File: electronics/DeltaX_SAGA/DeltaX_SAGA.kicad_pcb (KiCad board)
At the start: 4 copper layers, 50 x 50 mm, 76 parts, among them J1 USB_B_Micro, J10 Motor3_Encoder, J11 M12, J12 M21, J13 M22, J14 M31, J15 M33, J16 Thrower+, J17 Thrower-, J2 Programmer, J3 SERVO, J4 M11, J5 Battery+, J6 Thrower Signal, J7 Battery-, J8 Motor1_Encoder, J9 Motor2_Encoder, Q1 BUK6Y10, U1 CM1223, U10 DRV8243, U11 DRV8243, U2 NCP164C, U3 STM32G441KB, U4 NCV8730, U5 TPS62933, U6 MAX14930, U7 MAX14930, U8 MAX12930, U9 DRV8243

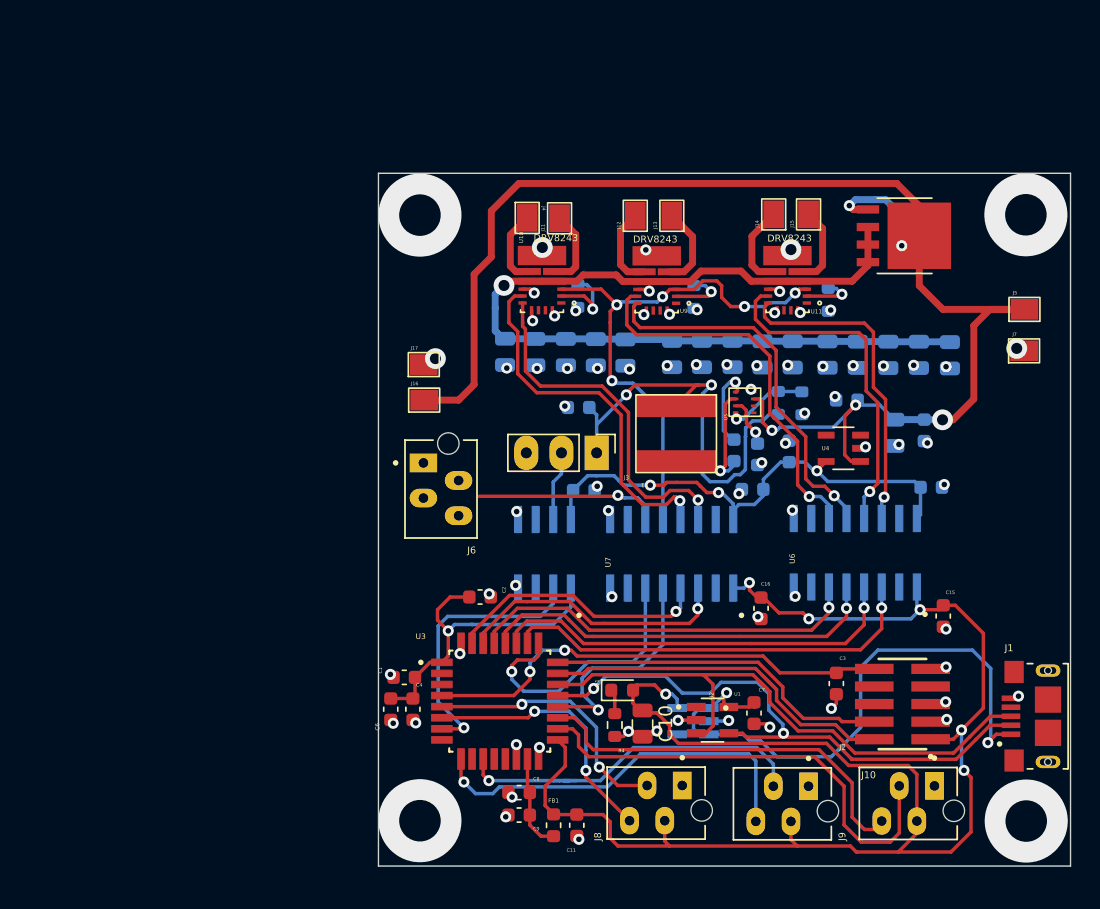
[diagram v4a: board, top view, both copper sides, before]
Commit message: PCB design updated and complete design added
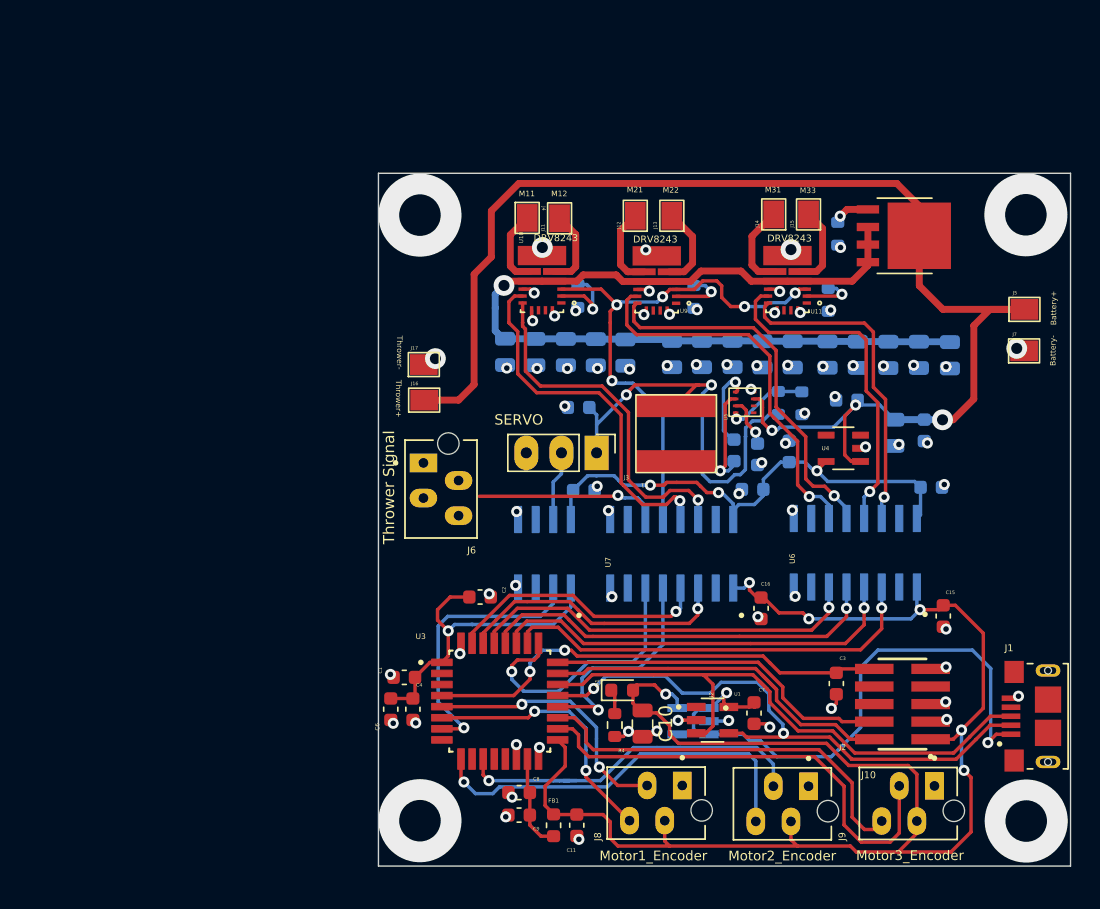
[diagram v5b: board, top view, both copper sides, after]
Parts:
- moved R3 4.37 mm to (159.2, 87.1)
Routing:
- net Net-(Q1-Pad4): track 6.17 -> 2.72 mm
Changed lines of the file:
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@@
       (effects (font (size 0.5 0.5) (thickness 0.075)))
     )
-    (fp_text value "Motor1_Encoder" (at -2.092 5.08 180) (layer "F.Fab")
+    (fp_text value "Motor1_Encoder" (at -2.092 5.08 180) (layer "F.SilkS")
       (effects (font (size 0.7 0.7) (thickness 0.12)))
     )
@@
       (effects (font (size 0.5 0.5) (thickness 0.1)))
     )
-    (fp_text value "Thrower Signal" (at -1.7625 -2.4859 90) (layer "F.Fab")
+    (fp_text value "Thrower Signal" (at -1.7625 -2.4859 90) (layer "F.SilkS")
       (effects (font (size 0.8 0.8) (thickness 0.15)))
     )
@@
       (effects (font (size 0.3 0.3) (thickness 0.075)))
     )
-    (fp_text value "SERVO" (at -1.905 2.5504 180) (layer "F.Fab")
+    (fp_text value "SERVO" (at -2.3876 5.6238 180) (layer "F.SilkS")
       (effects (font (size 0.75 0.75) (thickness 0.15)))
     )
@@
       (effects (font (size 0.25 0.25) (thickness 0.0625)))
     )
-    (fp_text value "Thrower+" (at -1.905 -0.0762 270 unlocked) (layer "F.Fab")
+    (fp_text value "Thrower+" (at -1.905 -0.0762 270 unlocked) (layer "F.SilkS")
       (effects (font (size 0.4 0.4) (thickness 0.1)))
     )
@@
     )
     (fp_text value "LED" (at -2.286 0.508) (layer "F.Fab")
-      (effects (font (size 0.5 0.5) (thickness 0.125)))
+      (effects (font (size 0.5 0.5) (thickness 0.125) italic))
     )
     (fp_text user "${REFERENCE}" (at 0 0) (layer "F.Fab")
@@
       (effects (font (size 0.25 0.25) (thickness 0.0625)))
     )
-    (fp_text value "Thrower-" (at -1.8034 -0.8382 270 unlocked) (layer "F.Fab")
+    (fp_text value "Thrower-" (at -1.8034 -0.8382 270 unlocked) (layer "F.SilkS")
       (effects (font (size 0.4 0.4) (thickness 0.1)))
     )
@@
       (effects (font (size 0.25 0.25) (thickness 0.0625)))
     )
-    (fp_text value "M11" (at -1.8034 0.0508 unlocked) (layer "F.Fab")
+    (fp_text value "M11" (at -1.8034 0.0508 unlocked) (layer "F.SilkS")
       (effects (font (size 0.4 0.4) (thickness 0.1)))
     )
@@
       (effects (font (size 0.5 0.5) (thickness 0.125)))
     )
-    (fp_text value "Motor3_Encoder" (at -1.7625 5.0325) (layer "F.Fab")
+    (fp_text value "Motor3_Encoder" (at -1.7625 5.0325) (layer "F.SilkS")
       (effects (font (size 0.7 0.7) (thickness 0.12)))
     )
@@
       (effects (font (size 0.25 0.25) (thickness 0.0625)))
     )
-    (fp_text value "Battery-" (at 2.032 0 90 unlocked) (layer "F.Fab")
+    (fp_text value "Battery-" (at 2.032 0 90 unlocked) (layer "F.SilkS")
       (effects (font (size 0.4 0.4) (thickness 0.1)))
     )
@@
       (effects (font (size 0.25 0.25) (thickness 0.0625)))
     )
-    (fp_text value "M33" (at 1.6764 -0.0254 unlocked) (layer "F.Fab")
+    (fp_text value "M33" (at 1.6764 -0.0254 unlocked) (layer "F.SilkS")
       (effects (font (size 0.4 0.4) (thickness 0.1)))
     )
@@
       (effects (font (size 0.25 0.25) (thickness 0.0625)))
     )
-    (fp_text value "M21" (at 1.8288 0 unlocked) (layer "F.Fab")
+    (fp_text value "M21" (at 1.8288 0 unlocked) (layer "F.SilkS")
       (effects (font (size 0.4 0.4) (thickness 0.1)))
     )
@@
       (effects (font (size 0.25 0.25) (thickness 0.0625)))
     )
-    (fp_text value "M22" (at 1.8034 -0.0508 unlocked) (layer "F.Fab")
+    (fp_text value "M22" (at 1.8034 -0.0508 unlocked) (layer "F.SilkS")
       (effects (font (size 0.4 0.4) (thickness 0.1)))
     )
@@
       (effects (font (size 0.25 0.25) (thickness 0.0625)))
     )
-    (fp_text value "M31" (at 1.7272 -0.0254 unlocked) (layer "F.Fab")
+    (fp_text value "M31" (at 1.7272 -0.0254 unlocked) (layer "F.SilkS")
       (effects (font (size 0.4 0.4) (thickness 0.1)))
     )
@@
       (effects (font (size 0.25 0.25) (thickness 0.0625)))
     )
-    (fp_text value "Battery+" (at 2.0574 -0.0762 90 unlocked) (layer "F.Fab")
+    (fp_text value "Battery+" (at 2.0574 -0.0762 90 unlocked) (layer "F.SilkS")
       (effects (font (size 0.4 0.4) (thickness 0.1)))
     )
@@
       (effects (font (size 0.5 0.5) (thickness 0.125)))
     )
-    (fp_text value "Motor2_Encoder" (at -1.9025 5.0325) (layer "F.Fab")
+    (fp_text value "Motor2_Encoder" (at -1.9025 5.0325) (layer "F.SilkS")
       (effects (font (size 0.7 0.7) (thickness 0.12)))
     )
@@
       (effects (font (size 0.25 0.25) (thickness 0.0625)))
     )
-    (fp_text value "M12" (at 1.7272 0 unlocked) (layer "F.Fab")
+    (fp_text value "M12" (at 1.7272 0 unlocked) (layer "F.SilkS")
       (effects (font (size 0.4 0.4) (thickness 0.1)))
     )
@@
   )
   (footprint "Resistor_SMD:R_0603_1608Metric" (layer "B.Cu")
-    (at 163.5252 86.9696 -90)
+    (at 159.1564 87.0712 -90)
     (descr "Resistor SMD 0603 (1608 Metric), square (rectangular) end terminal, IPC_7351 nominal, (Body size source: IPC-SM-782 page 72, https://www.pcb-3d.com/wordpress/wp-content/uploads/ipc-sm-782a_amendment_1_and_2.pdf), generated with kicad-footprint-generator")
     (tags "resistor")
@@
   (via (at 137.235232 91.345499) (size 0.8) (drill 0.4) (layers "F.Cu" "B.Cu") (net 5))
   (via (at 138.708659 93.004616) (size 0.8) (drill 0.4) (layers "F.Cu" "B.Cu") (net 5))
+  (via (at 159.3596 88.0618) (size 0.8) (drill 0.4) (layers "F.Cu" "B.Cu") (net 5))
   (via (at 139.446 99.5172) (size 0.8) (drill 0.4) (layers "F.Cu" "B.Cu") (net 5))
   (via (at 154.9654 91.2368) (size 0.8) (drill 0.4) (layers "F.Cu" "B.Cu") (net 5))
@@
   (via (at 164.6428 96.5708) (size 0.8) (drill 0.4) (layers "F.Cu" "B.Cu") (net 5))
   (via (at 145.542 91.2114) (size 0.8) (drill 0.4) (layers "F.Cu" "B.Cu") (net 5))
-  (via (at 163.7792 87.9348) (size 0.8) (drill 0.4) (layers "F.Cu" "B.Cu") (net 5))
   (via (at 140.2334 92.6338) (size 0.8) (drill 0.4) (layers "F.Cu" "B.Cu") (net 5))
   (via (at 145.158298 92.909202) (size 0.8) (drill 0.4) (layers "F.Cu" "B.Cu") (net 5))
@@
   (segment (start 155.7122 96.7334) (end 155.5496 96.5708) (width 0.5) (layer "B.Cu") (net 5))
   (segment (start 167.259 96.7994) (end 167.1066 96.7994) (width 0.5) (layer "B.Cu") (net 5))
-  (segment (start 163.639 87.7946) (end 163.7792 87.9348) (width 0.25) (layer "B.Cu") (net 5))
   (segment (start 159.0418 98.904761) (end 158.963359 98.82632) (width 0.25) (layer "B.Cu") (net 5))
   (segment (start 155.9814 107.1372) (end 155.8798 107.0356) (width 0.25) (layer "B.Cu") (net 5))
   (segment (start 158.4198 96.7486) (end 158.1912 96.7486) (width 0.5) (layer "B.Cu") (net 5))
+  (segment (start 159.1564 87.8962) (end 159.194 87.8962) (width 0.5) (layer "B.Cu") (net 5))
   (segment (start 163.2458 102.3976) (end 163.4642 102.3976) (width 0.25) (layer "B.Cu") (net 5))
   (segment (start 155.9052 96.7334) (end 155.7122 96.7334) (width 0.5) (layer "B.Cu") (net 5))
   (segment (start 158.1912 96.7486) (end 158.0896 96.647) (width 0.5) (layer "B.Cu") (net 5))
   (segment (start 160.6042 96.7588) (end 160.4366 96.7588) (width 0.5) (layer "B.Cu") (net 5))
+  (segment (start 159.194 87.8962) (end 159.3596 88.0618) (width 0.5) (layer "B.Cu") (net 5))
   (segment (start 162.814 96.769) (end 162.6058 96.769) (width 0.5) (layer "B.Cu") (net 5))
   (segment (start 152.2346 105.537) (end 152.2346 105.6262) (width 0.25) (layer "B.Cu") (net 5))
@@
   (segment (start 143.8148 96.6064) (end 143.8758 96.6064) (width 0.25) (layer "B.Cu") (net 5))
   (segment (start 166.6878 105.3462) (end 166.8526 105.1814) (width 0.25) (layer "B.Cu") (net 5))
-  (segment (start 163.5252 87.7946) (end 163.639 87.7946) (width 0.25) (layer "B.Cu") (net 5))
   (segment (start 156.5656 100.139) (end 156.655 100.139) (width 0.25) (layer "B.Cu") (net 5))
   (segment (start 143.8758 96.6064) (end 144.1196 96.8502) (width 0.25) (layer "B.Cu") (net 5))
@@
   (segment (start 165.0238 94.869) (end 167.2286 94.869) (width 0.5) (layer "B.Cu") (net 87))
   (segment (start 134.9908 94.6556) (end 134.5184 94.1832) (width 0.5) (layer "B.Cu") (net 87))
-  (segment (start 161.3366 85.31355) (end 160.26895 85.31355) (width 0.5) (layer "F.Cu") (net 88))
-  (segment (start 160.26895 85.31355) (end 159.9946 85.0392) (width 0.5) (layer "F.Cu") (net 88))
-  (via (at 159.9946 85.0392) (size 0.8) (drill 0.4) (layers "F.Cu" "B.Cu") (net 88))
-  (segment (start 162.6108 84.6074) (end 161.8234 84.6074) (width 0.5) (layer "B.Cu") (net 88))
-  (segment (start 163.5252 86.1446) (end 163.5252 85.5218) (width 0.5) (layer "B.Cu") (net 88))
-  (segment (start 163.5252 85.5218) (end 163.0426 85.0392) (width 0.5) (layer "B.Cu") (net 88))
-  (segment (start 161.8234 84.6074) (end 160.4264 84.6074) (width 0.5) (layer "B.Cu") (net 88))
-  (segment (start 163.0426 85.0392) (end 162.6108 84.6074) (width 0.5) (layer "B.Cu") (net 88))
-  (segment (start 160.4264 84.6074) (end 159.9946 85.0392) (width 0.5) (layer "B.Cu") (net 88))
+  (segment (start 159.82185 85.31355) (end 159.3342 85.8012) (width 0.5) (layer "F.Cu") (net 88))
+  (segment (start 161.3366 85.31355) (end 159.82185 85.31355) (width 0.5) (layer "F.Cu") (net 88))
+  (via (at 159.3342 85.8012) (size 0.8) (drill 0.4) (layers "F.Cu" "B.Cu") (net 88))
+  (segment (start 159.1564 86.2462) (end 159.1564 85.979) (width 0.5) (layer "B.Cu") (net 88))
+  (segment (start 159.1564 85.979) (end 159.3342 85.8012) (width 0.5) (layer "B.Cu") (net 88))
   (segment (start 128.626 119.112) (end 128.626 120.484) (width 0.25) (layer "F.Cu") (net 89))
   (segment (start 144.3737 120.9927) (end 145.0594 121.6784) (width 0.25) (layer "F.Cu") (net 89))

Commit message: updated PCB design
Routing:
- net /Thrower_PWM_Isolated: track 13.3 -> 15.3 mm
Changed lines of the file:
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@@
   (segment (start 147.8026 114.1222) (end 147.7264 114.1984) (width 0.25) (layer "B.Cu") (net 38))
   (segment (start 147.7264 114.1984) (end 147.574 114.3508) (width 0.25) (layer "B.Cu") (net 38))
-  (segment (start 143.2168 106.0334) (end 133.2688 106.0334) (width 0.25) (layer "F.Cu") (net 43))
   (segment (start 143.2814 105.9688) (end 143.2168 106.0334) (width 0.25) (layer "F.Cu") (net 43))
+  (segment (start 132.9132 106.0334) (end 131.7719 104.8921) (width 0.25) (layer "F.Cu") (net 43))
+  (segment (start 143.2168 106.0334) (end 132.9132 106.0334) (width 0.25) (layer "F.Cu") (net 43))
   (via (at 143.2814 105.9688) (size 0.8) (drill 0.4) (layers "F.Cu" "B.Cu") (net 43))
   (segment (start 144.8308 106.2736) (end 144.7038 106.1466) (width 0.25) (layer "B.Cu") (net 43))

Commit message: PCB design updated
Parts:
- removed C12: 1uF, Capacitor_SMD:C_0603_1608Metric
- removed C13: 1nF, Capacitor_SMD:C_0603_1608Metric
- removed U4: NCV8730, NCV8730:SOT95P275X110-5N
- C15, C3, Q1: moved to B.Cu
- C27: footprint Capacitor_SMD:C_0603_1608Metric -> Capacitor_SMD:C_1206_3216Metric
- moved J7 44.1 mm to (128.9, 90.8), turned to 180 degrees
- moved J5 43.9 mm to (128.8, 93.4), turned to 180 degrees
- moved Q1 27.1 mm to (137.1, 89.7)
- moved R3 21.3 mm to (137.9, 86.2), turned to 180 degrees
- moved U1 17.9 mm to (168.0, 121.4), turned to -90 degrees
- moved C23 16.9 mm to (146.4, 100.8)
- moved C24 16.7 mm to (148.7, 100.6)
- moved J13 10.1 mm to (157.2, 85.4)
- moved R10 9.95 mm to (158.7, 92.3)
- moved J15 9.76 mm to (166.8, 85.4)
- moved U9 9.63 mm to (155.7, 90.2)
- moved R12 9.61 mm to (168.0, 92.7)
- moved U11 9.50 mm to (165.0, 90.2)
- moved J12 9.50 mm to (154.0, 85.4)
- moved J14 8.72 mm to (163.2, 85.4)
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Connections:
- C18 pad 2: +5VA -> +5VD
- C19 pad 2: +5VA -> +5VD
- C23 pad 1: /V+ -> /VM
- C24 pad 1: /V+ -> /VM
- C5 pad 1: +5VA -> +5VD
- J1 pad : (no net) -> unconnected-(J1-Pad6)
- U5 pad 3: /V+ -> /VM
- U6 pad 16: +5VA -> +5VD
- U7 pad 16: +5VA -> +5VD
- U8 pad 8: +5VA -> +5VD
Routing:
- net /V+: track 98.3 -> 38.8 mm, vias 3 -> 25
- net +5VA: track 37.0 -> 0.00 mm, vias 3 -> 0
- net +5VD: track 32.4 -> 64.7 mm, vias 2 -> 4
- net /VM: track 67.4 -> 43.2 mm, vias 1 -> 13
- net +3.3V: track 142.6 -> 163.2 mm, vias 7 -> 5
- net /Motor3_PWM_Isolated: track 24.6 -> 17.6 mm
- net /Motor3_DIR_Isolated: track 23.4 -> 16.7 mm
- net /Motor3_OUT1: track 6.16 -> 0.00 mm
- net /Motor2_OUT2: track 5.98 -> 0.00 mm
- net /Motor3_OUT2: track 5.92 -> 0.00 mm
- net /Motor2_OUT1: track 5.89 -> 0.00 mm
- net /SWDIO: track 27.1 -> 21.2 mm
- net /Motor1_OUT2: track 5.65 -> 0.00 mm
- net /Motor1_OUT1: track 5.52 -> 0.00 mm
- net GND: track 20.1 -> 14.8 mm, vias 25 -> 24
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- added copper zone on F.Cu, net /Motor1_OUT1
- added copper zone on F.Cu, net /Motor1_OUT2
- added copper zone on F.Cu, net /Motor2_OUT1
- added copper zone on F.Cu, net /Motor2_OUT2
- added copper zone on F.Cu, net /Motor3_OUT1
- added copper zone on F.Cu, net /Motor3_OUT2
- added copper zone on F.Cu, net /V+
- added copper zone on B.Cu, net /VM
- added copper zone on B.Cu, net GND

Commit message: PCB board updated
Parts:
- C15, C18, C19, C3, C5: moved to F.Cu
- L1, U2, U5, U6, U7, U8: moved to B.Cu
- moved C11 29.5 mm to (169.4, 125.0)
- moved FB1 29.5 mm to (167.8, 125.0)
- moved C8 29.1 mm to (165.2, 127.5)
- moved C9 29.1 mm to (165.2, 129.1)
- moved C6 27.3 mm to (153.9, 117.6)
- moved C4 27.3 mm to (155.5, 117.6)
- moved U3 26.9 mm to (161.7, 120.9)
- moved C1 26.7 mm to (154.3, 115.2)
- moved C23 18.1 mm to (164.5, 101.4), turned to 90 degrees
- moved C27 16.1 mm to (156.4, 101.7), turned to 180 degrees
- moved C7 14.1 mm to (138.0, 123.2), turned to 180 degrees
- moved C24 13.8 mm to (162.5, 101.6), turned to 90 degrees
- moved C16 11.5 mm to (143.1, 111.0), turned to 0 degrees
- moved C15 11.4 mm to (157.9, 111.5), turned to 0 degrees
- moved C18 11.1 mm to (158.2, 105.7)
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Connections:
- C26 pad 1: Net-(C26-Pad1) -> Net-(U5-Pad6)
- J1 pad : unconnected-(J1-Pad6) -> (no net)
- L1 pad 1: Net-(C26-Pad1) -> Net-(C26-Pad2)
- U5 pad 6: Net-(C26-Pad1) -> Net-(U5-Pad6)
- U6 pad 11: /Motor2_PWM_Isolated -> /Motor3_DIR_Isolated
- U6 pad 12: /Motor2_DIR_Isolated -> /Motor3_PWM_Isolated
- U6 pad 13: /Motor3_PWM_Isolated -> /Motor2_DIR_Isolated
- U6 pad 14: /Motor3_DIR_Isolated -> /Motor2_PWM_Isolated
- U6 pad 3: /Motor3_DIR -> /Motor2_PWM
- U6 pad 4: /Motor3_PWM -> /Motor2_DIR
- U6 pad 5: /Motor2_DIR -> /Motor3_PWM
- U6 pad 6: /Motor2_PWM -> /Motor3_DIR
- U7 pad 11: /Thrower_PWM_Isolated -> /Motor1_DIR_Isolated
- U7 pad 12: /nSLEEP_Isolated -> /Motor1_PWM_Isolated
- U7 pad 13: /Motor1_PWM_Isolated -> /nSLEEP_Isolated
- U7 pad 14: /Motor1_DIR_Isolated -> /Thrower_PWM_Isolated
- U7 pad 3: /Motor1_DIR -> /Thrower_PWM
- U7 pad 4: /Motor1_PWM -> /nSLEEP
- U7 pad 5: /nSLEEP -> /Motor1_PWM
- U7 pad 6: /Thrower_PWM -> /Motor1_DIR
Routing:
- net /USB_D-: track 39.0 -> 7.06 mm, vias 2 -> 0
- net +5V: track 44.2 -> 12.8 mm, vias 3 -> 0
- net /USB_D+: track 37.8 -> 6.98 mm, vias 2 -> 0
- net /NRST: track 36.1 -> 8.54 mm, vias 3 -> 0
- net +3.3V: track 163.2 -> 135.8 mm, vias 5 -> 4
- net /Motor3_DIR: track 32.2 -> 7.12 mm, vias 1 -> 0
- net /Motor3_PWM: track 31.4 -> 6.93 mm, vias 1 -> 0
- net /Motor2_DIR: track 31.0 -> 6.74 mm, vias 1 -> 0
- net /Motor2_PWM: track 30.4 -> 6.54 mm, vias 1 -> 0
- net /Motor3_ENCA: track 33.9 -> 15.9 mm, vias 0 -> 1
- net +5VD: track 64.7 -> 49.8 mm, vias 4 -> 10
- net /Motor1_PWM_Isolated: track 22.3 -> 7.51 mm, vias 1 -> 0
- net GND: track 14.8 -> 0.00 mm, vias 24 -> 0
- net /Motor1_DIR_Isolated: track 22.0 -> 8.50 mm, vias 1 -> 0
- net /Servo_PWM: track 19.8 -> 32.2 mm, vias 1 -> 2
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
